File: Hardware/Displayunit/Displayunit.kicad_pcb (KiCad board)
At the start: 4 copper layers, 155 x 69.8 mm, 143 parts, among them IC1 TSC2007, IC2 MX25LM51245GXDI00, IC3 IS66WVH8M8BLL-100B1LI_0, IC4 TPS61165DRVR, J1 615008138221, J10 ER-CON10HT-1, J11 Conn_02x03_Odd_Even, J2 615008138221, J3 54104-4031, J4 Conn_ARM_JTAG_SWD_20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

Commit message: Lengthmatch OctoSPI again Remove leftover traces General cleanup
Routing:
- net OctoSPI_P2_IO0: track 50.6 -> 45.0 mm
- net OctoSPI_P2_IO5: track 49.8 -> 45.0 mm
- net +3.3VA: track 40.5 -> 35.9 mm, vias 8 -> 7
- net OctoSPI_P2_IO4: track 49.2 -> 45.0 mm
- net OctoSPI_P1_IO7: track 50.1 -> 47.0 mm
- net I2C2_SCL: track 93.7 -> 91.0 mm
- net I2C2_SDA: track 86.1 -> 83.7 mm, vias 7 -> 6
- net LCD_LED-K: track 83.4 -> 81.9 mm
- net Net-(C27-Pad2): track 43.1 -> 41.7 mm
- net LCD_B0: track 52.0 -> 50.8 mm
- net SPI1_SCK: track 29.3 -> 30.5 mm
- net SPI1_MOSI: track 29.6 -> 30.8 mm
- net Net-(BT1-Pad1): track 42.4 -> 43.5 mm
- net +3V3: track 231.4 -> 232.4 mm
- net LCD_B5: track 41.8 -> 40.8 mm
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
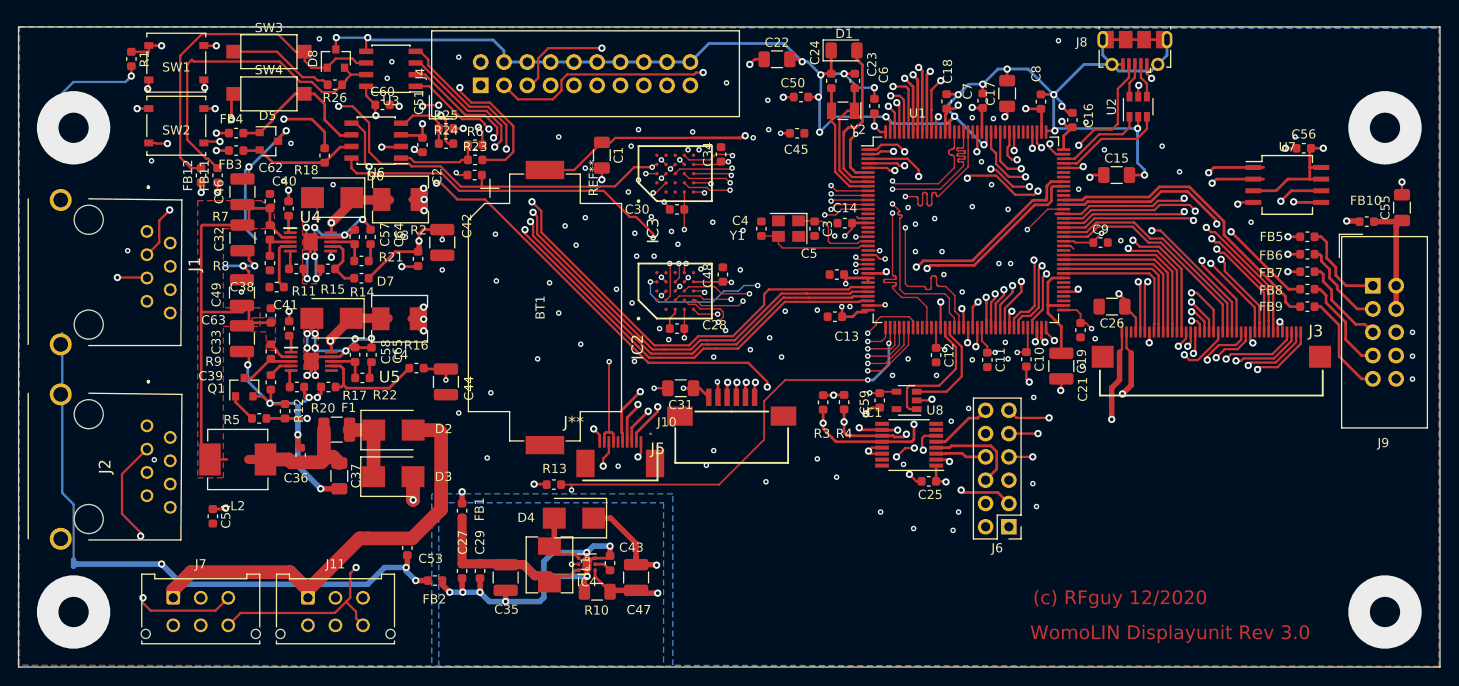
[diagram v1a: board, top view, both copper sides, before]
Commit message: Problem Vermischung mit V1 Layoutdaten gefixt, Octo SPI Längenmatching. V3 Produktionsdaten für JCLPCB erzeugt.
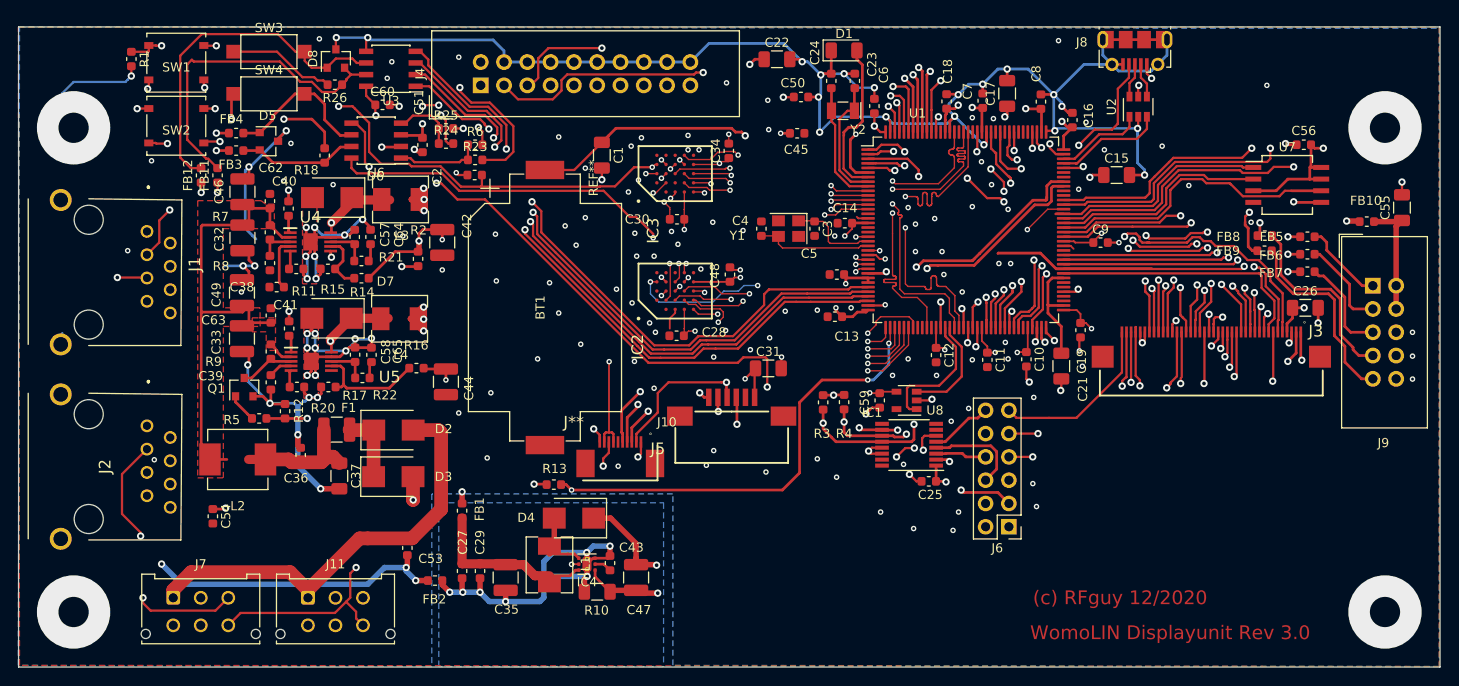
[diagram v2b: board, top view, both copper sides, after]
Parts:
- C21: footprint Capacitor_SMD:C_1210_3225Metric -> Capacitor_SMD:C_1206_3216Metric
- moved C26 21.1 mm to (202.3, 79.6), turned to 0 degrees
- moved C31 9.80 mm to (143.8, 86.2), turned to 0 degrees
- moved FB9 7.68 mm to (197.9, 73.4)
- moved FB8 7.47 mm to (197.9, 71.8)
- moved C30 1.08 mm to (133.8, 70.0)
- moved C34 0.93 mm to (139.4, 62.5)
- moved C28 0.78 mm to (133.8, 82.7)
- moved C48 0.77 mm to (139.6, 76.0)
- moved C56 0.38 mm to (202.1, 61.8)
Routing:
- net LCD_R4: track 16.8 -> 63.3 mm, vias 0 -> 2
- net GND: track 438.6 -> 410.5 mm
- net LCD_R2: track 19.5 -> 39.1 mm
- net LCD_LED-K: track 81.9 -> 100.0 mm
- net LCD_40: track 36.8 -> 19.1 mm, vias 2 -> 0
- net LCD_LED-A: track 82.1 -> 98.9 mm
- net LCD_39: track 37.5 -> 21.8 mm
- net LCD_38: track 39.8 -> 25.3 mm
- net LCD_R0: track 49.0 -> 62.3 mm
- net LCD_R3: track 16.0 -> 28.7 mm
- net LCD_R1: track 49.7 -> 61.6 mm, vias 2 -> 4
- net LCD_G2: track 28.8 -> 40.3 mm
- net LCD_37: track 40.3 -> 29.2 mm
- net LCD_R5: track 17.6 -> 28.4 mm, vias 0 -> 2
- net Net-(FB9-Pad1): track 11.6 -> 21.5 mm
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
